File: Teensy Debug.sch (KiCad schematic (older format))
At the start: 3 parts, among them J1 Conn_02x07_Odd_Even, U1 MKL02Z32VFG4, U2 MKL02Z32VFG4

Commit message: V2
Changed from generic header to Cortex-M 9 pin debug header.
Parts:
- removed J1: Conn_02x07_Odd_Even, Connector_PinHeader_2.54mm:PinHeader_2x07_P2.54mm_Vertical, symbol Connector_Generic:Conn_02x07_Odd_Even
- added J1: FTSH-105-XX-X-DV, SAMTEC_FTSH-105-XX-X-DV, symbol FTSH-105-XX-X-DV:FTSH-105-XX-X-DV
- added JP1, JP2, JP3, JP4, JP5: SolderJumper_2_Open, Jumper:SolderJumper-2_P1.3mm_Open_Pad1.0x1.5mm, symbol Jumper:SolderJumper_2_Open
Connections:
- wire segments 80 -> 94
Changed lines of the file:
@@
-$EndComp
-$Comp
-L Connector_Generic:Conn_02x07_Odd_Even J1
-U 1 1 5FF34813
-P 9300 4300
-F 0 "J1" H 9350 4817 50  0000 C CNN
-F 1 "Conn_02x07_Odd_Even" H 9350 4726 50  0000 C CNN
-F 2 "Connector_PinHeader_2.54mm:PinHeader_2x07_P2.54mm_Vertical" H 9300 4300 50  0001 C CNN
-F 3 "~" H 9300 4300 50  0001 C CNN
-	1    9300 4300
-	1    0    0    -1
 $EndComp
 $Comp
@@
 	2750 4400 5100 4400
 Wire Wire Line
-	5100 4400 5100 4600
-Wire Wire Line
-	5100 4600 9100 4600
-Wire Wire Line
-	2750 1300 10950 1300
-Wire Wire Line
-	10950 1300 10950 4600
-Wire Wire Line
-	10950 4600 9600 4600
-Wire Wire Line
-	9600 4600 9600 4750
-Wire Wire Line
-	9600 4750 9100 4750
-Wire Wire Line
-	9100 4750 9100 4600
-Connection ~ 9600 4600
-Connection ~ 9100 4600
-Wire Wire Line
-	9100 4500 9000 4500
-Wire Wire Line
-	9000 4500 9000 4850
-Wire Wire Line
-	9000 4850 10600 4850
-Wire Wire Line
-	10600 4850 10600 4500
-Wire Wire Line
-	10600 4500 9600 4500
-Wire Wire Line
-	9000 4850 5100 4850
-Wire Wire Line
-	5100 4850 5100 7200
-Wire Wire Line
-	5100 7200 2750 7200
-Connection ~ 9000 4850
+	2750 1300 5100 1300
+Wire Wire Line
+	4750 7200 2750 7200
 Connection ~ 2750 7200
 Wire Wire Line
-	2750 4100 5300 4100
-Wire Wire Line
-	5300 4100 5300 4500
-Wire Wire Line
-	5300 4500 9000 4500
-Connection ~ 9000 4500
-Wire Wire Line
 	1450 2800 850  2800
 Wire Wire Line
@@
 	850  1150 10700 1150
 Wire Wire Line
-	10700 1150 10700 4300
-Wire Wire Line
-	10700 4300 9600 4300
+	10700 1150 10700 3500
 Wire Wire Line
 	850  4300 850  5900
@@
 	800  1100 11050 1100
 Wire Wire Line
-	11050 1100 11050 4200
-Wire Wire Line
-	11050 4200 9600 4200
+	11050 1100 11050 3200
+Wire Wire Line
+	11050 3200 10400 3200
 Wire Wire Line
 	1450 5700 800  5700
@@
 	4050 2100 10600 2100
 Wire Wire Line
-	10600 2100 10600 4100
-Wire Wire Line
-	10600 4100 9600 4100
-Wire Wire Line
-	9100 4100 5750 4100
+	10600 2100 10600 3300
+Wire Wire Line
+	6950 4100 5750 4100
 Wire Wire Line
 	5750 5200 4050 5200
@@
 	5750 4100 5750 5200
 Wire Wire Line
-	800  4200 9100 4200
+	800  4200 6800 4200
 Wire Wire Line
 	4050 2600 10500 2600
 Wire Wire Line
-	10500 2600 10500 4400
-Wire Wire Line
-	10500 4400 9600 4400
-Wire Wire Line
-	9100 4400 5950 4400
-Wire Wire Line
-	5950 4400 5950 5700
+	10500 2600 10500 5150
+Wire Wire Line
+	10500 5150 9600 5150
+Wire Wire Line
+	5950 5150 5950 5700
 Wire Wire Line
 	5950 5700 4050 5700
@@
 	1350 900  10850 900
 Wire Wire Line
-	10850 900  10850 4000
-Wire Wire Line
-	10850 4000 9600 4000
+	10850 900  10850 3400
+Wire Wire Line
+	10850 3400 10200 3400
 Wire Wire Line
 	1450 5800 1250 5800
@@
 	1250 7450 6150 7450
 Wire Wire Line
-	6150 7450 6150 4000
-Wire Wire Line
-	6150 4000 9100 4000
-Wire Wire Line
-	850  4300 9100 4300
-Text Notes 8400 4650 0    50   ~ 0
+	6150 7450 6150 3950
+Wire Wire Line
+	850  4300 6650 4300
+Text Notes 8400 3250 0    50   ~ 0
 VTref
-Text Notes 8400 4550 0    50   ~ 0
-GND
-Text Notes 8400 4350 0    50   ~ 0
+Text Notes 8400 4900 0    50   ~ 0
 TDI
-Text Notes 8400 4250 0    50   ~ 0
+Text Notes 8400 4600 0    50   ~ 0
 TMS
-Text Notes 8400 4150 0    50   ~ 0
+Text Notes 8400 4300 0    50   ~ 0
 TCK
-Text Notes 8400 4450 0    50   ~ 0
+Text Notes 8400 5200 0    50   ~ 0
 MOD
-Text Notes 8400 4050 0    50   ~ 0
+Text Notes 8400 4000 0    50   ~ 0
 TDO
-Text Notes 10050 4650 0    50   ~ 0
-VTref
-Text Notes 10050 4550 0    50   ~ 0
-GND
-Text Notes 10050 4350 0    50   ~ 0
+Text Notes 9950 3550 0    50   ~ 0
 TDI
-Text Notes 10050 4250 0    50   ~ 0
+Text Notes 9950 3250 0    50   ~ 0
 TMS
-Text Notes 10050 4150 0    50   ~ 0
+Text Notes 9950 3350 0    50   ~ 0
 TCK
-Text Notes 10050 4450 0    50   ~ 0
-MOD
-Text Notes 10050 4050 0    50   ~ 0
+Text Notes 9950 3450 0    50   ~ 0
 TDO
 Text Notes 2850 5650 2    50   ~ 0
@@
 Text Notes 3650 5750 2    50   ~ 0
 (MOD) AD_B0_08
+Text Notes 10050 5200 0    50   ~ 0
+MOD
+Wire Wire Line
+	2650 4100 2750 4100
+Connection ~ 2750 4100
+Text Notes 8400 3350 0    50   ~ 0
+GND
+Wire Wire Line
+	2750 4100 4750 4100
+Wire Wire Line
+	4750 4100 4750 7200
+Connection ~ 4750 4100
+Wire Wire Line
+	4750 3300 4750 4100
+Wire Wire Line
+	8750 3400 8850 3400
+Wire Wire Line
+	5100 4400 5100 3200
+Wire Wire Line
+	5100 3200 8850 3200
+Wire Wire Line
+	5100 3200 5100 1300
+Connection ~ 5100 3200
+Wire Wire Line
+	10400 4550 10400 3200
+Connection ~ 10400 3200
+Wire Wire Line
+	10400 3200 9850 3200
+Wire Wire Line
+	10600 3300 10300 3300
+Wire Wire Line
+	10700 3500 10100 3500
+Wire Wire Line
+	10300 4250 10300 3300
+Connection ~ 10300 3300
+Wire Wire Line
+	10300 3300 9850 3300
+Wire Wire Line
+	10200 3950 10200 3400
+Connection ~ 10200 3400
+Wire Wire Line
+	10200 3400 9850 3400
+Wire Wire Line
+	10100 4850 10100 3500
+Connection ~ 10100 3500
+Wire Wire Line
+	10100 3500 9850 3500
+Wire Wire Line
+	8750 3400 8750 5350
+Wire Wire Line
+	8750 5350 9600 5350
+Wire Wire Line
+	9600 5350 9600 5150
+$Comp
+L FTSH-105-XX-X-DV:FTSH-105-XX-X-DV J1
+U 1 1 60B58083
+P 9350 3400
+F 0 "J1" H 9350 3867 50  0000 C CNN
+F 1 "FTSH-105-XX-X-DV" H 9350 3776 50  0000 C CNN
+F 2 "SAMTEC_FTSH-105-XX-X-DV" H 9350 3400 50  0001 L BNN
+F 3 "" H 9350 3400 50  0001 L BNN
+F 4 "H" H 9350 3400 50  0001 L BNN "PARTREV"
+F 5 "Samtec" H 9350 3400 50  0001 L BNN "MANUFACTURER"
+F 6 "Manufacturer Recommendation" H 9350 3400 50  0001 L BNN "STANDARD"
+	1    9350 3400
+	1    0    0    -1
+$EndComp
+Wire Wire Line
+	4750 3300 8850 3300
+$Comp
+L Jumper:SolderJumper_2_Open JP4
+U 1 1 60BBBD93
+P 9350 4850
+F 0 "JP4" H 9350 5055 50  0000 C CNN
+F 1 "SolderJumper_2_Open" H 9350 4964 50  0000 C CNN
+F 2 "Jumper:SolderJumper-2_P1.3mm_Open_Pad1.0x1.5mm" H 9350 4850 50  0001 C CNN
+F 3 "~" H 9350 4850 50  0001 C CNN
+	1    9350 4850
+	1    0    0    -1
+$EndComp
+$Comp
+L Jumper:SolderJumper_2_Open JP3
+U 1 1 60BCAB53
+P 9350 4550
+F 0 "JP3" H 9350 4755 50  0000 C CNN
+F 1 "SolderJumper_2_Open" H 9350 4664 50  0000 C CNN
+F 2 "Jumper:SolderJumper-2_P1.3mm_Open_Pad1.0x1.5mm" H 9350 4550 50  0001 C CNN
+F 3 "~" H 9350 4550 50  0001 C CNN
+	1    9350 4550
+	1    0    0    -1
+$EndComp
+$Comp
+L Jumper:SolderJumper_2_Open JP2
+U 1 1 60BCB2B3
+P 9350 4250
+F 0 "JP2" H 9350 4455 50  0000 C CNN
+F 1 "SolderJumper_2_Open" H 9350 4364 50  0000 C CNN
+F 2 "Jumper:SolderJumper-2_P1.3mm_Open_Pad1.0x1.5mm" H 9350 4250 50  0001 C CNN
+F 3 "~" H 9350 4250 50  0001 C CNN
+	1    9350 4250
+	1    0    0    -1
+$EndComp
+$Comp
+L Jumper:SolderJumper_2_Open JP1
+U 1 1 60BCB988
+P 9350 3950
+F 0 "JP1" H 9350 4155 50  0000 C CNN
+F 1 "SolderJumper_2_Open" H 9350 4064 50  0000 C CNN
+F 2 "Jumper:SolderJumper-2_P1.3mm_Open_Pad1.0x1.5mm" H 9350 3950 50  0001 C CNN
+F 3 "~" H 9350 3950 50  0001 C CNN
+	1    9350 3950
+	1    0    0    -1
+$EndComp
+$Comp
+L Jumper:SolderJumper_2_Open JP5
+U 1 1 60BCE665
+P 9350 5150
+F 0 "JP5" H 9350 5355 50  0000 C CNN
+F 1 "SolderJumper_2_Open" H 9350 5264 50  0000 C CNN
+F 2 "Jumper:SolderJumper-2_P1.3mm_Open_Pad1.0x1.5mm" H 9350 5150 50  0001 C CNN
+F 3 "~" H 9350 5150 50  0001 C CNN
+	1    9350 5150
+	1    0    0    -1
+$EndComp
+Wire Wire Line
+	5950 5150 9200 5150
+Wire Wire Line
+	9500 5150 9600 5150
+Connection ~ 9600 5150
+Wire Wire Line
+	6650 4300 6650 4850
+Wire Wire Line
+	6650 4850 9200 4850
+Wire Wire Line
+	9500 4850 10100 4850
+Wire Wire Line
+	9500 4550 10400 4550
+Wire Wire Line
+	6800 4200 6800 4550
+Wire Wire Line
+	6800 4550 9200 4550
+Wire Wire Line
+	6950 4100 6950 4250
+Wire Wire Line
+	6950 4250 9200 4250
+Wire Wire Line
+	9500 4250 10300 4250
+Wire Wire Line
+	6150 3950 9200 3950
+Wire Wire Line
+	9500 3950 10200 3950
 $EndSCHEMATC

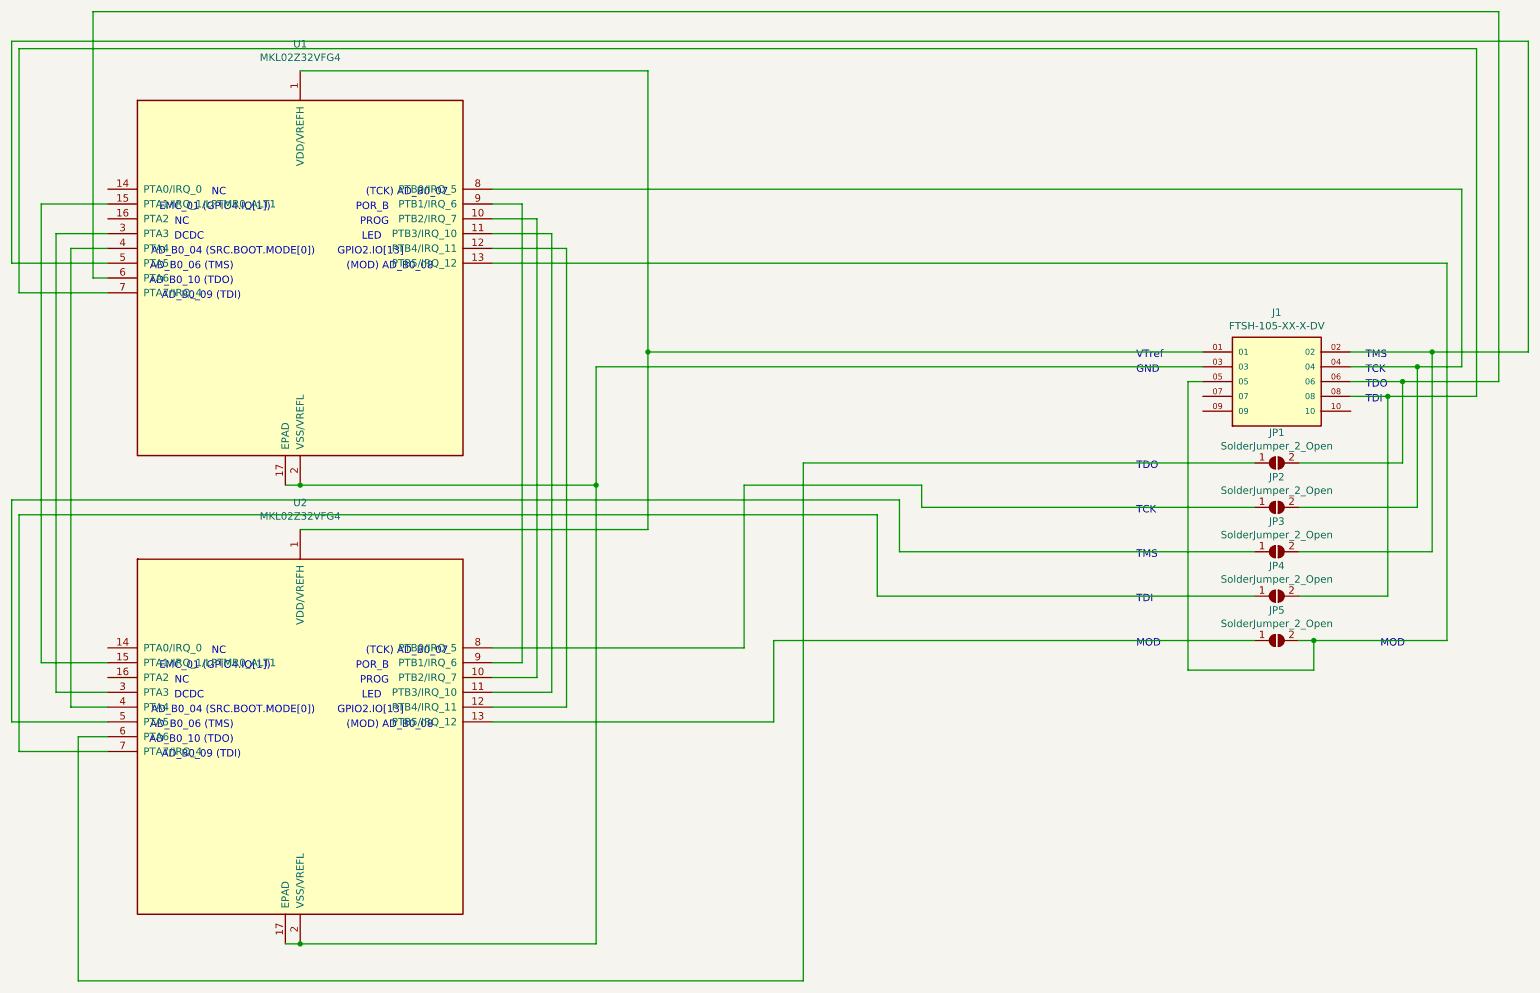
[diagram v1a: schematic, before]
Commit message: Mini Version
Removed Cortex M0, replaced with Attiny10, flex pcb fits within the size of the Teensy 4.1
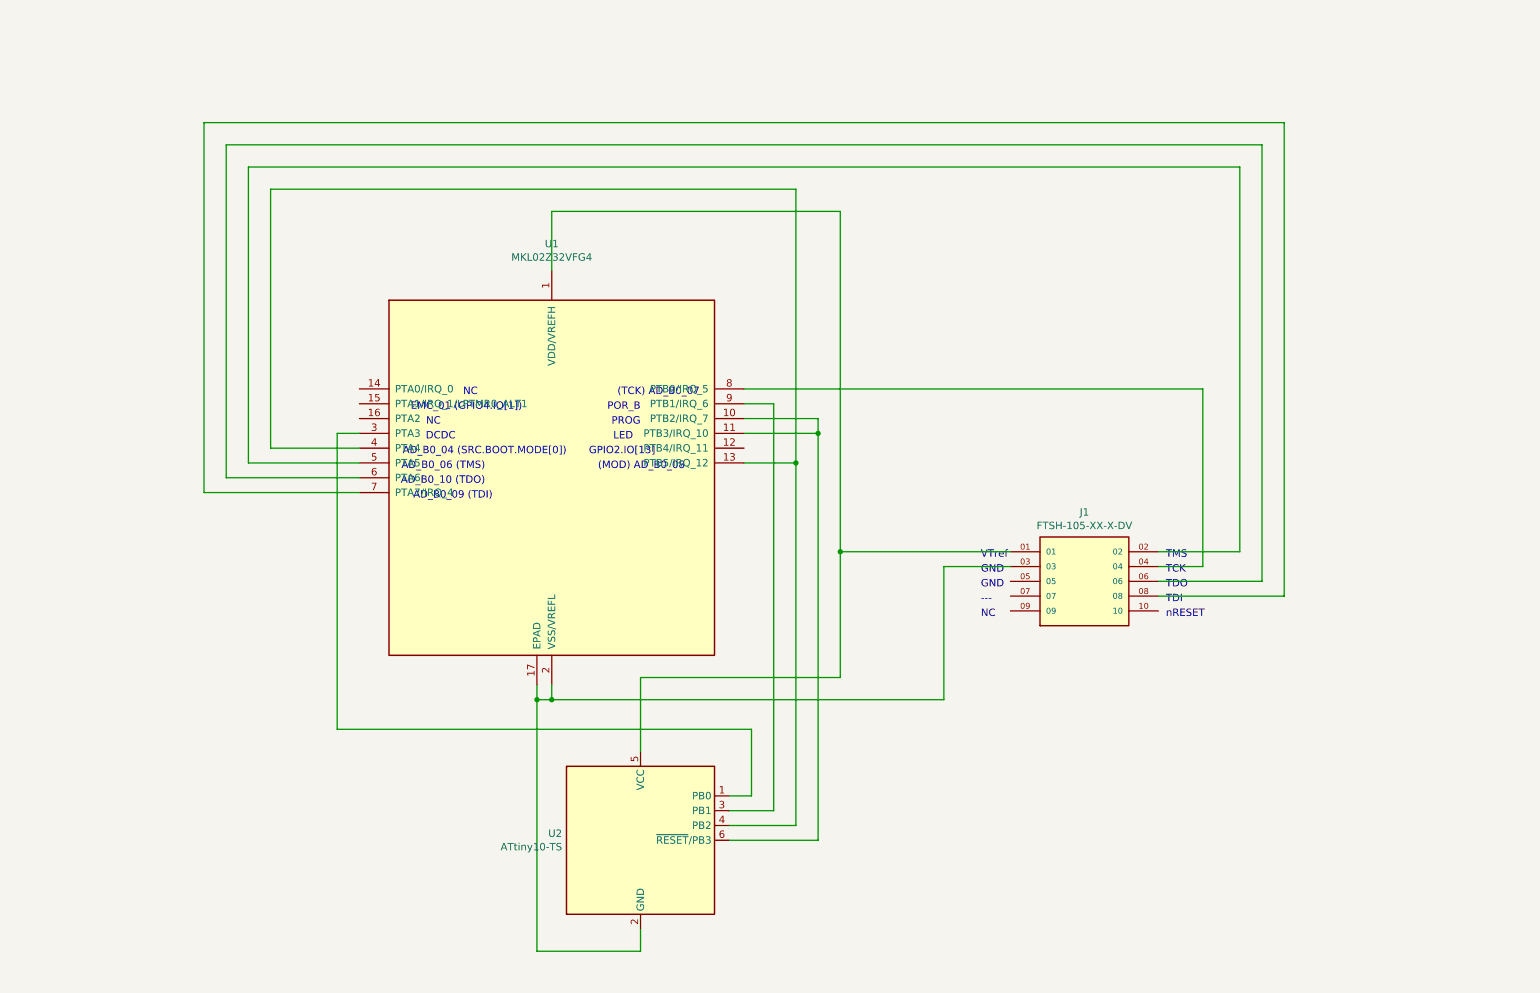
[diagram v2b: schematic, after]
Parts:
- removed JP1, JP2, JP3, JP4, JP5: SolderJumper_2_Open, Jumper:SolderJumper-2_P1.3mm_Open_Pad1.0x1.5mm, symbol Jumper:SolderJumper_2_Open
- removed U2: MKL02Z32VFG4, Package_DFN_QFN:QFN-16-1EP_3x3mm_P0.5mm_EP1.9x1.9mm, symbol MCU_NXP_Kinetis:MKL02Z32VFG4
- added U2: ATtiny10-TS, Package_TO_SOT_SMD:SOT-23-6, symbol MCU_Microchip_ATtiny:ATtiny10-TS
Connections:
- net at J1.01, U1.1 (VDD/VREFH): now also U2.5 (VCC)
- net at U1.10 (PTB2/IRQ_7): now also U1.11 (PTB3/IRQ_10), U2.6 (~RESET~/PB3)
- net at U1.13 (PTB5/IRQ_12): now also U1.4 (PTA4), U2.4 (PB2); no longer J1.05
- net at J1.03, U1.17 (EPAD), U1.2 (VSS/VREFL): now also U2.2 (GND)
- net at U1.3 (PTA3): now also U2.1 (PB0)
- net at U1.9 (PTB1/IRQ_6): now also U2.3 (PB1)
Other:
- note added: "---"
- note added: "nRESET"
- note removed: "MOD"
- moved on the sheet: J1, U1
